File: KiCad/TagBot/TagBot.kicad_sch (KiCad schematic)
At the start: 52 parts, among them IC101 ADXL343BCCZ-RL, J101 Conn_ST_STDC14, J102 Conn_01x06, J103 Conn_01x03, J104 Conn_01x06, J105 Conn_01x02, J106 Conn_01x08, J107 Conn_01x06, J111 Conn_01x04, SW101 SW_Push, SW102 SW_Push, U101 STM32G431CBUx, Y101 Crystal

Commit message: correction schema kicad
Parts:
- removed C107: 100n, Capacitor_SMD:C_0402_1005Metric, symbol Device:C
- removed D101, D102, D103, D104: LED, LED_SMD:LED_0603_1608Metric, symbol Device:LED
- removed J102, J104, J107: Conn_01x06, Connector_JST:JST_XH_S6B-XH-A_1x06_P2.50mm_Horizontal, symbol Connector_Generic:Conn_01x06
- removed J106: Conn_01x08, Connector_JST:JST_XH_S8B-XH-A_1x08_P2.50mm_Horizontal, symbol Connector_Generic:Conn_01x08
- removed J111: Conn_01x04, Connector_JST:JST_XH_S4B-XH-A_1x04_P2.50mm_Horizontal, symbol Connector_Generic:Conn_01x04
- removed JP101, JP102, JP103: SolderJumper_2_Open, Jumper:SolderJumper-2_P1.3mm_Open_TrianglePad1.0x1.5mm, symbol Jumper:SolderJumper_2_Open
- removed R101: 1.3k, Resistor_SMD:R_0402_1005Metric, symbol Device:R
- removed R102, R103, R104: 100, Resistor_SMD:R_0402_1005Metric, symbol Device:R
- removed R105, R106: 100k, Resistor_SMD:R_0402_1005Metric, symbol Device:R_Small
- removed R108, R109: 1k, Resistor_SMD:R_0402_1005Metric, symbol Device:R_Small
- removed R111, R112, R113, R114: 100, Resistor_SMD:R_0402_1005Metric, symbol Device:R_Small
- removed SW101, SW102: SW_Push, Button_Switch_SMD:SW_Push_1P1T_NO_6x6mm_H9.5mm, symbol Switch:SW_Push
- added C107: 100n, Capacitor_SMD:C_0402_1005Metric, symbol Device:C_Small
- added L101: 47n, Inductor_SMD:L_0402_1005Metric, symbol Device:L_Small
- C108, C111: value 100n -> 1u
- C112: value 100n -> 10n
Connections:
- net +3.3V: now also L101.1; no longer C108.1, C108.2, U101.20 (VREF+), U101.21 (VDDA)
- net BTN_CAT_MOUSE: no longer C112.1
- net GND: now also C108.1, C111.1, C112.1, C107.1; no longer C111.2, C112.2
- net NRST: no longer C111.1
- new net +3.3VA: C107.2, C108.2, C111.2, C112.2, L101.2, U101.20 (VREF+), U101.21 (VDDA)
- no-connect marks 8 -> 7
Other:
- added sheet Boutons (bouton.kicad_sch)
- added sheet Capteur bords (capteurBords.kicad_sch)
- added sheet Ecran (ecran.kicad_sch)
- added sheet LED (led.kicad_sch)
- added sheet Lidar (lidar.kicad_sch)
- added sheet Moteurs (moteurs.kicad_sch)
- note removed: "LIDAR"
- note removed: "capteurs fin de bords"
- note removed: "doit-on ajouter un AOP entre capteurs et stm ? (dépasse 3.6V ?)"
- note removed: "moteurs (left)"
- note removed: "moteurs (right)"
- note removed: "écran"
- moved on the sheet: C101, C102, C103, C104, C105, C106, IC101

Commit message: placement pcb 2
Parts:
- L101: value 47n -> 39n; footprint Inductor_SMD:L_0402_1005Metric -> Inductor_SMD:L_0603_1608Metric
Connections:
- net +3.3V: no longer C101.1, C102.1
- net GND: now also C101.1, C102.1
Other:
- moved on the sheet: C101, C102

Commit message: update routage
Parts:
- removed C101, C102: 1u, Capacitor_SMD:C_0402_1005Metric, symbol Device:C_Small
- removed IC101: ADXL343BCCZ-RL, ADXL343BCCZ-RL:ADXL343BCCZRL, symbol ADXL343BCCZ-RL:ADXL343BCCZ-RL
- added C1, C2: 1u, Capacitor_SMD:C_0603_1608Metric, symbol Device:C_Small
- added U1: ADXL343, Package_LGA:LGA-14_3x5mm_P0.8mm_LayoutBorder1x6y, symbol Sensor_Motion:ADXL343
- C103, C108, C111: footprint Capacitor_SMD:C_0402_1005Metric -> Capacitor_SMD:C_0603_1608Metric
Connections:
- net +3.3V: now also C1.2, C2.2, U1.1 (Vdd_I/O), U1.6 (Vs)
- net CS-NSS: now also U1.7 (~{CS})
- net GND: now also C1.1, C2.1, U1.2 (GND), U1.4 (GND), U1.5 (GND)
- net Interrupt1: now also U1.8 (INT1)
- net Interrupt2: now also U1.9 (INT2)
- net SCLK-SCK: now also U1.14 (SCL/SCLK)
- net SDI-MOSI: now also U1.13 (SDA/SDI/SDIO)
- net SDO-MISO: now also U1.12 (SDO/ADDR)

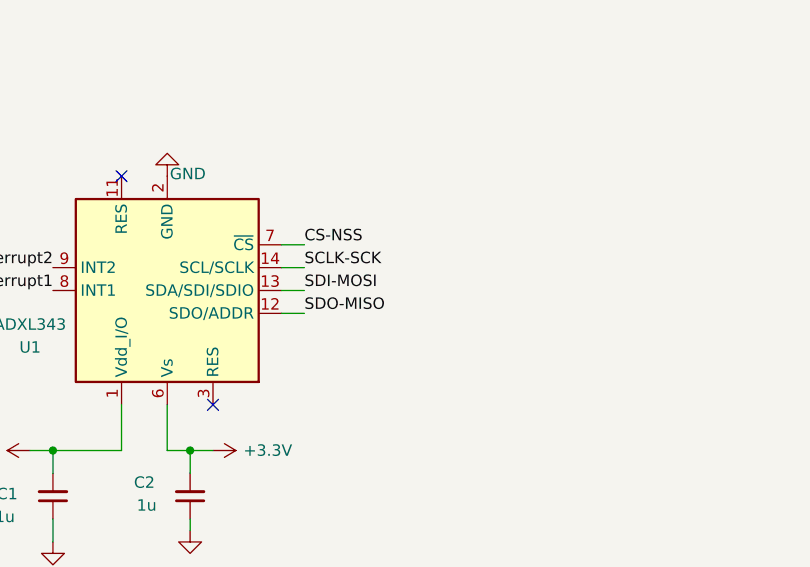
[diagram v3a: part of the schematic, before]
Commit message: correction routage
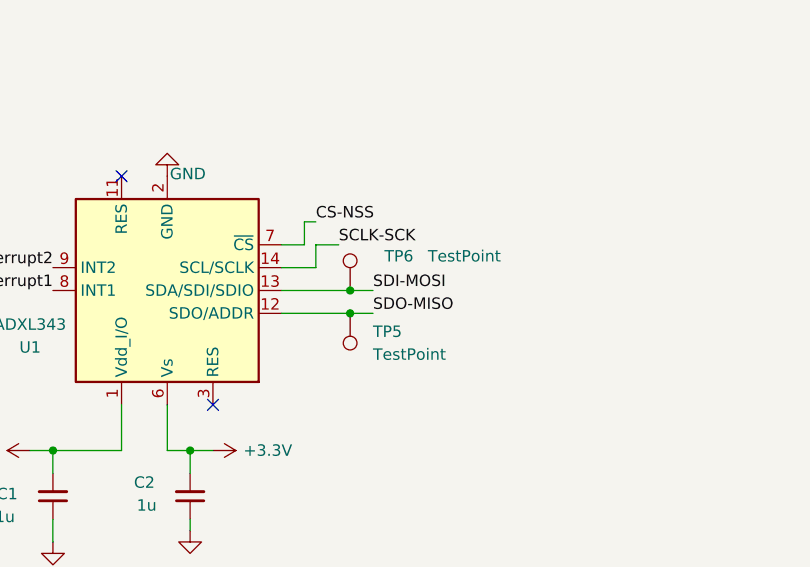
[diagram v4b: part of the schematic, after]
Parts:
- added TP5, TP6: TestPoint, TestPoint:TestPoint_Pad_D1.5mm, symbol Connector:TestPoint
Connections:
- net SDI-MOSI: now also TP6.1
- net SDO-MISO: now also TP5.1
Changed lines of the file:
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@@
 	)
 	(junction
+		(at 127 237.49)
+		(diameter 0)
+		(color 0 0 0 0)
+	)
+	(junction
 		(at 31.75 34.29)
 		(diameter 0)
@@
 	)
 	(junction
+		(at 127 240.03)
+		(diameter 0)
+		(color 0 0 0 0)
+	)
+	(junction
 		(at 38.1 26.67)
 		(diameter 0)
@@
 	(wire
 		(pts
+			(xy 127 237.49) (xy 119.38 237.49)
+		)
+		(stroke
+			(width 0)
+			(type default)
+		)
+	)
+	(wire
+		(pts
 			(xy 80.01 52.07) (xy 77.47 52.07)
 		)
@@
 	(wire
 		(pts
+			(xy 127 240.03) (xy 119.38 240.03)
+		)
+		(stroke
+			(width 0)
+			(type default)
+		)
+	)
+	(wire
+		(pts
 			(xy 142.24 41.91) (xy 142.24 40.64)
 		)
@@
 	(wire
 		(pts
+			(xy 121.92 232.41) (xy 119.38 232.41)
+		)
+		(stroke
+			(width 0)
+			(type default)
+		)
+	)
+	(wire
+		(pts
 			(xy 132.08 41.91) (xy 132.08 40.64)
 		)
@@
 	(wire
 		(pts
-			(xy 121.92 237.49) (xy 119.38 237.49)
+			(xy 129.54 237.49) (xy 127 237.49)
 		)
 		(stroke
@@
 	(wire
 		(pts
-			(xy 121.92 232.41) (xy 119.38 232.41)
+			(xy 123.19 229.87) (xy 121.92 229.87)
 		)
 		(stroke
@@
 	(wire
 		(pts
+			(xy 123.19 234.95) (xy 119.38 234.95)
+		)
+		(stroke
+			(width 0)
+			(type default)
+		)
+	)
+	(wire
+		(pts
 			(xy 67.31 25.4) (xy 67.31 26.67)
 		)
@@
 	(wire
 		(pts
-			(xy 119.38 234.95) (xy 121.92 234.95)
+			(xy 123.19 232.41) (xy 125.73 232.41)
 		)
 		(stroke
@@
 	(wire
 		(pts
-			(xy 121.92 240.03) (xy 119.38 240.03)
+			(xy 129.54 240.03) (xy 127 240.03)
 		)
 		(stroke
@@
 	(wire
 		(pts
+			(xy 123.19 232.41) (xy 123.19 234.95)
+		)
+		(stroke
+			(width 0)
+			(type default)
+		)
+	)
+	(wire
+		(pts
 			(xy 41.91 52.07) (xy 44.45 52.07)
 		)
@@
 	(wire
 		(pts
+			(xy 121.92 229.87) (xy 121.92 232.41)
+		)
+		(stroke
+			(width 0)
+			(type default)
+		)
+	)
+	(wire
+		(pts
 			(xy 121.92 41.91) (xy 121.92 40.64)
 		)
@@
 	)
 	(label "CS-NSS"
-		(at 121.92 232.41 0)
+		(at 123.19 229.87 0)
 		(fields_autoplaced yes)
 		(effects
@@
 	)
 	(label "SDI-MOSI"
-		(at 121.92 237.49 0)
+		(at 129.54 237.49 0)
 		(fields_autoplaced yes)
 		(effects
@@
 	)
 	(label "SCLK-SCK"
-		(at 121.92 234.95 0)
+		(at 125.73 232.41 0)
 		(fields_autoplaced yes)
 		(effects
@@
 	)
 	(label "SDO-MISO"
-		(at 121.92 240.03 0)
+		(at 129.54 240.03 0)
 		(fields_autoplaced yes)
 		(effects
@@
 	)
 	(symbol
+		(lib_id "Connector:TestPoint")
+		(at 127 240.03 180)
+		(unit 1)
+		(exclude_from_sim no)
+		(in_bom yes)
+		(on_board yes)
+		(dnp no)
+		(fields_autoplaced yes)
+		(property "Reference" "TP5"
+			(at 129.54 242.0619 0)
+			(effects
+				(font
+					(size 1.27 1.27)
+				)
+				(justify right)
+			)
+		)
+		(property "Value" "TestPoint"
+			(at 129.54 244.6019 0)
+			(effects
+				(font
+					(size 1.27 1.27)
+				)
+				(justify right)
+			)
+		)
+		(property "Footprint" "TestPoint:TestPoint_Pad_D1.5mm"
+			(at 121.92 240.03 0)
+			(effects
+				(font
+					(size 1.27 1.27)
+				)
+				(hide yes)
+			)
+		)
+		(property "Datasheet" "~"
+			(at 121.92 240.03 0)
+			(effects
+				(font
+					(size 1.27 1.27)
+				)
+				(hide yes)
+			)
+		)
+		(property "Description" "test point"
+			(at 127 240.03 0)
+			(effects
+				(font
+					(size 1.27 1.27)
+				)
+				(hide yes)
+			)
+		)
+		(pin "1"
+		)
+		(instances
+			(project "TagBot"
+				(path "/6db08f37-7cb3-4000-93f1-ba0d0ffbeb19"
+					(reference "TP5")
+					(unit 1)
+				)
+			)
+		)
+	)
+	(symbol
 		(lib_id "Mechanical:MountingHole_Pad")
 		(at 344.17 189.23 0)
@@
 					(unit 1)
 				)
+			)
+		)
+	)
+	(symbol
+		(lib_id "Connector:TestPoint")
+		(at 127 237.49 0)
+		(unit 1)
+		(exclude_from_sim no)
+		(in_bom yes)
+		(on_board yes)
+		(dnp no)
+		(property "Reference" "TP6"
+			(at 130.81 233.68 0)
+			(effects
+				(font
+					(size 1.27 1.27)
+				)
+				(justify left)
+			)
+		)
+		(property "Value" "TestPoint"
+			(at 135.636 233.68 0)
+			(effects
+				(font
+					(size 1.27 1.27)
+				)
+				(justify left)
+			)
+		)
+		(property "Footprint" "TestPoint:TestPoint_Pad_D1.5mm"
+			(at 132.08 237.49 0)
+			(effects
+				(font
+					(size 1.27 1.27)
+				)
+				(hide yes)
+			)
+		)
+		(property "Datasheet" "~"
+			(at 132.08 237.49 0)
+			(effects
+				(font
+					(size 1.27 1.27)
+				)
+				(hide yes)
+			)
+		)
+		(property "Description" "test point"
+			(at 127 237.49 0)
+			(effects
+				(font
+					(size 1.27 1.27)
+				)
+				(hide yes)
+			)
+		)
+		(pin "1"
+		)
+		(instances
+			(project "TagBot"
+				(path "/6db08f37-7cb3-4000-93f1-ba0d0ffbeb19"
+					(reference "TP6")
+					(unit 1)
+				)

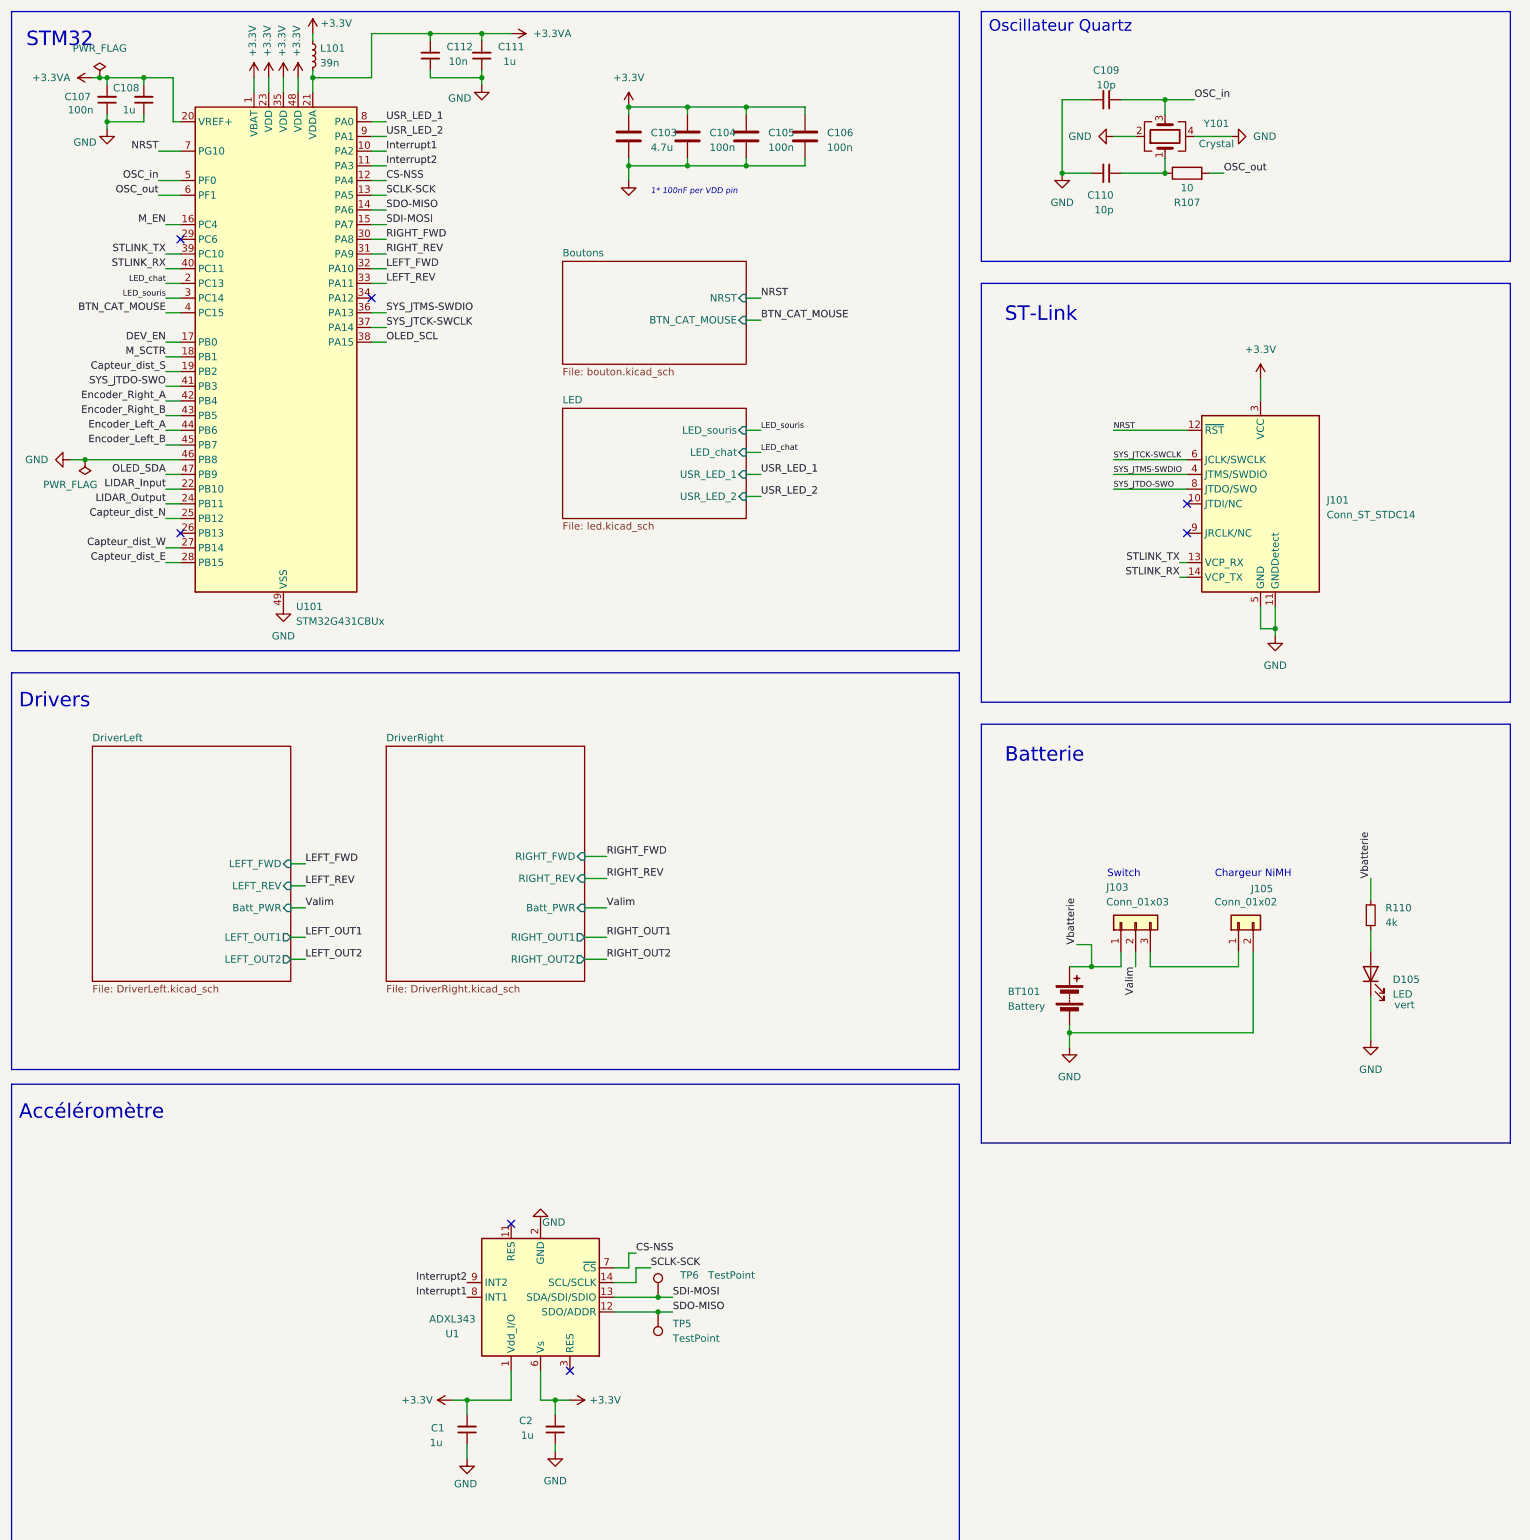
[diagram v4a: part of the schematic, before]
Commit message: fixed switch footprint and genrated gerber files
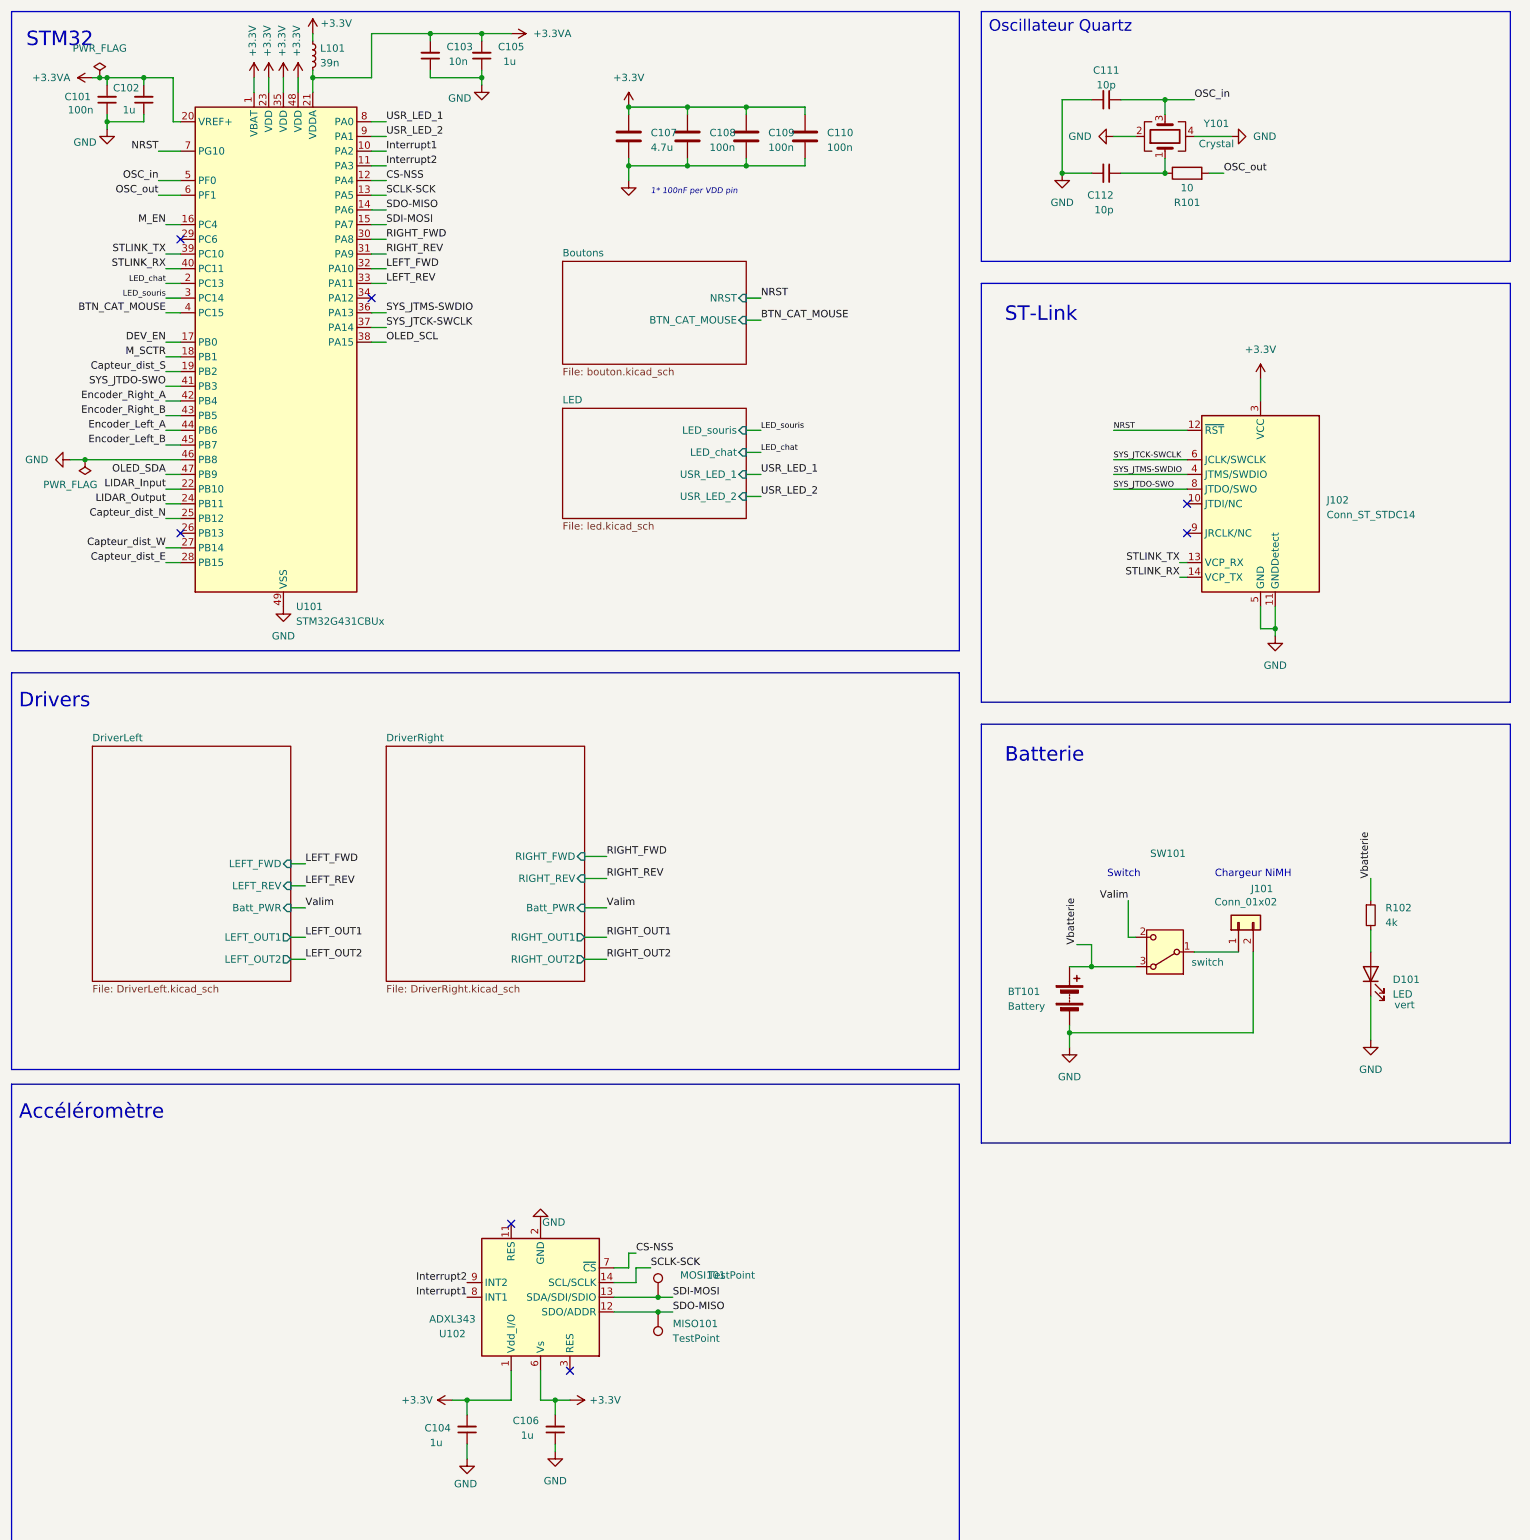
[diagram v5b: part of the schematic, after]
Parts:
- removed J103: Conn_01x03, Connector_JST:JST_XH_S3B-XH-A_1x03_P2.50mm_Horizontal, symbol Connector_Generic:Conn_01x03
- added SW101: switch, wurth_472121020311:472121020311, symbol Switch:SW_SPDT_312
- renumbered C107 to C101, C108 to C102, C112 to C103, C1 to C104, C111 to C105, C2 to C106, C103 to C107, C104 to C108, C105 to C109, C106 to C110, C109 to C111, C110 to C112, D105 to D101, J105 to J101, J101 to J102, TP5 to MISO101, TP6 to MOSI101, R107 to R101, R110 to R102, U1 to U102
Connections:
- net Valim: now also SW101.2 (C)
- net Vbatterie: now also SW101.3 (A)
- net at J101.1 (Pin_1): now also SW101.1 (B)
